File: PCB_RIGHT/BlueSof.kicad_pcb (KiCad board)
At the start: 2 copper layers, 134.8 x 98.3 mm, 88 parts, among them J1 USB_C_Receptacle_USB2.0, J12 SM02B-SRSS-TB_LF__SN_, Q2 A03407, SW1 SW_PUSH, SW10 SW_PUSH, SW11 SW_PUSH, SW12 SW_PUSH, SW13 SW_PUSH, SW14 SW_PUSH, SW15 SW_PUSH, SW16 SW_PUSH, SW17 SW_PUSH, SW18 SW_PUSH, SW19 SW_PUSH, SW2 SW_PUSH, SW20 SW_PUSH, SW21 SW_PUSH, SW22 SW_PUSH, SW23 SW_PUSH, SW24 SW_PUSH, SW25 Rotary_Encoder_Switch, SW26 SW_PUSH, SW27 SW_PUSH, SW28 SW_PUSH, SW3 SW_PUSH, SW4 SW_PUSH, SW5 SW_PUSH, SW6 SW_PUSH, SW7 SW_PUSH, SW8 SW_PUSH, SW9 SW_PUSH, U1 LN2054Y42AMR, U2 E73-2G4M08S1C, U3 AP2112K-3.3, Y1 32.768kHz

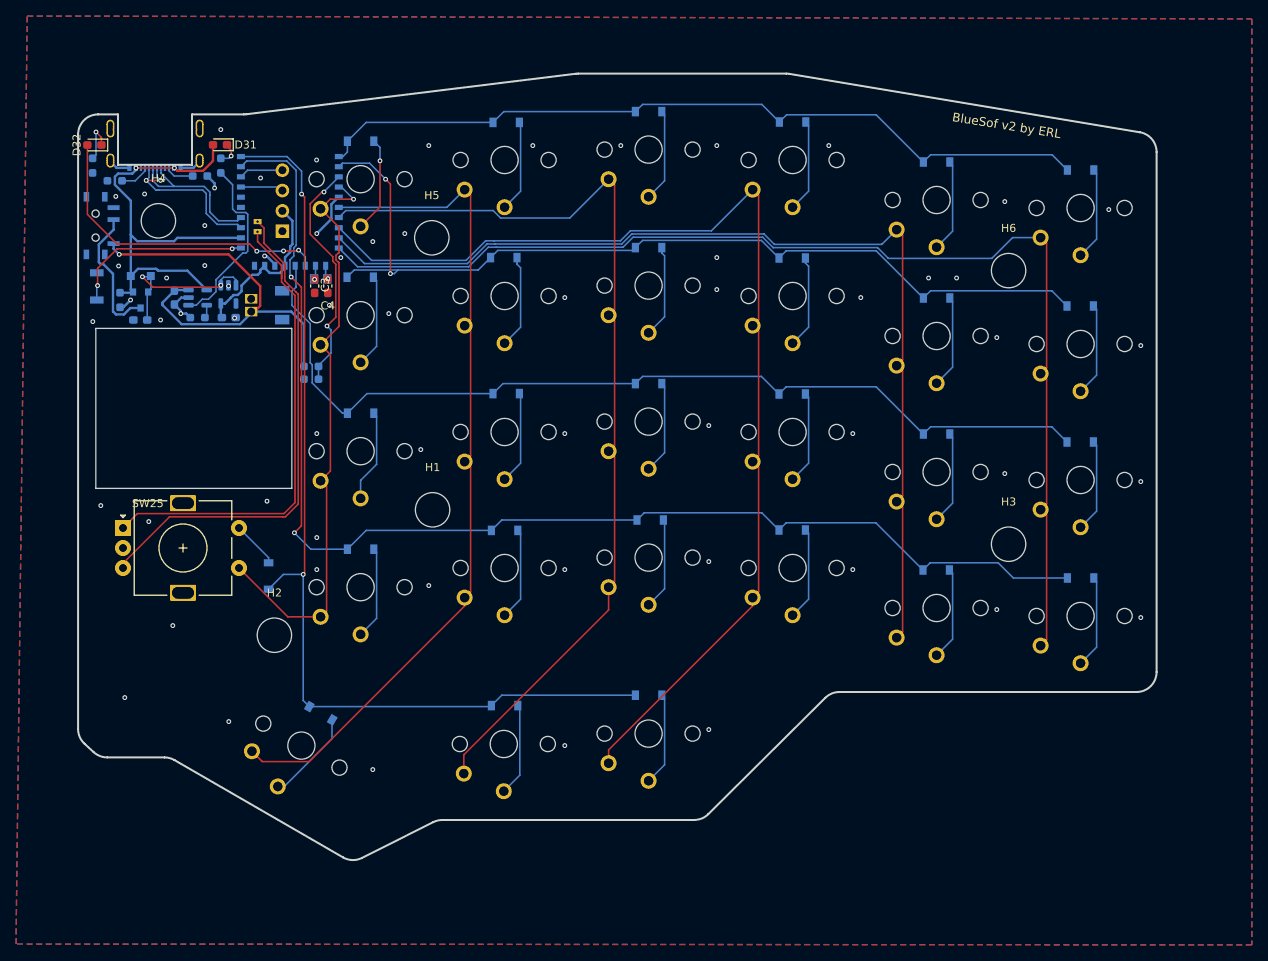
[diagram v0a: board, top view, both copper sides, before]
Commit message: ordered left side from jlc
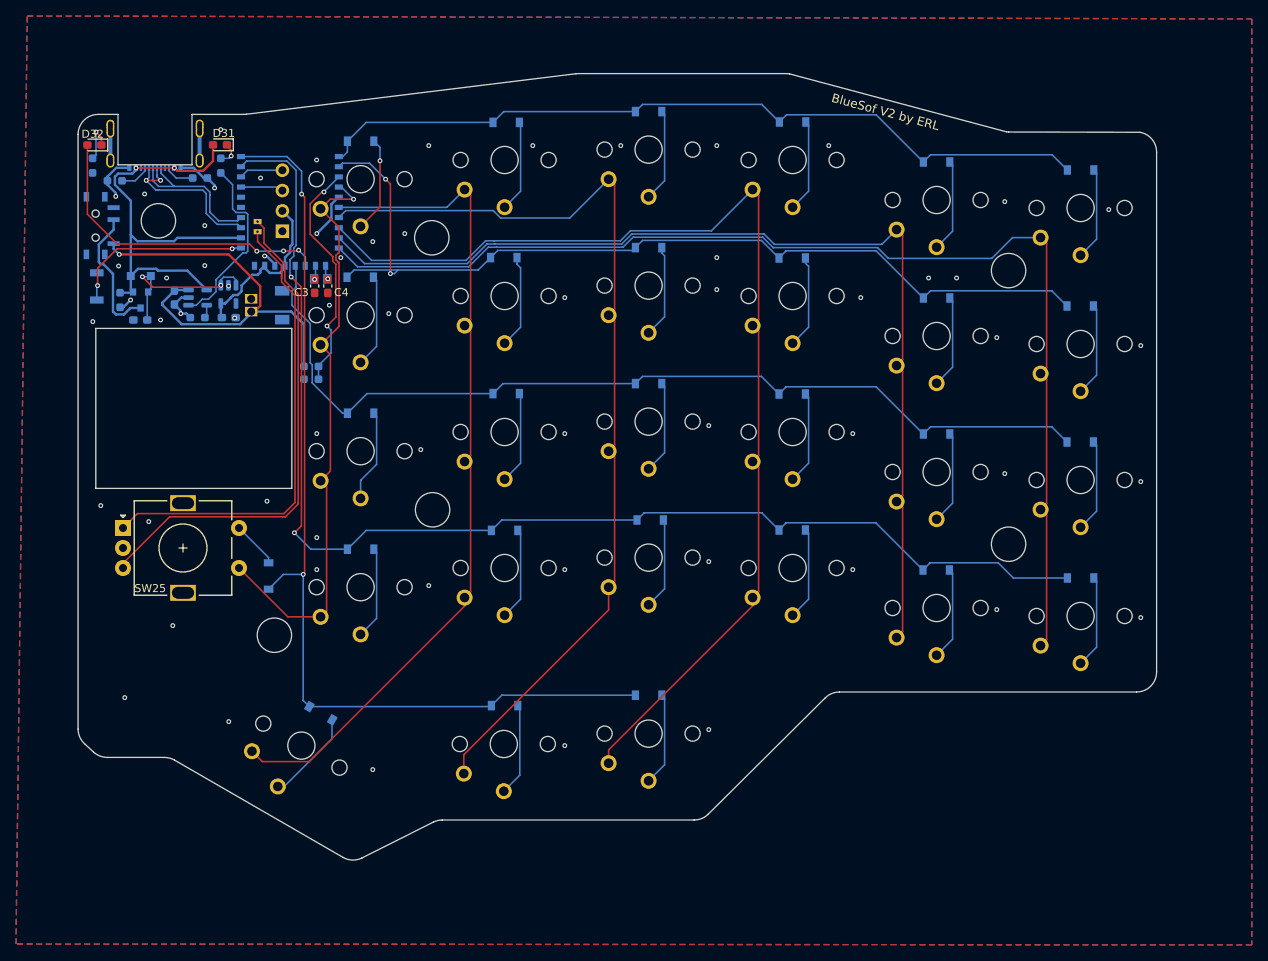
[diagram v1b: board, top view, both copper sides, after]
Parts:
- J12: value SM02B-SRSS-TB_LF__SN_ -> SM02B-SRSS-TB(LF)(SN)
- moved R8 0.25 mm to (101.4, 54.0)
- renumbered BATT1 to BATT_SW, RESET1 to RESET
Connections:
- net DATA+ renamed D+
- net DATA- renamed D-
- BATT_SW pad 3: no_connect_72 -> unconnected-(BATT1-Pad3)
- H1 pad 1: Net-(H1-Pad1) -> unconnected-(H1-Pad1)
- H2 pad 1: Net-(H2-Pad1) -> unconnected-(H2-Pad1)
- H3 pad 1: Net-(H3-Pad1) -> unconnected-(H3-Pad1)
- H4 pad 1: Net-(H4-Pad1) -> unconnected-(H4-Pad1)
- H5 pad 1: Net-(H5-Pad1) -> unconnected-(H5-Pad1)
- H6 pad 1: Net-(H6-Pad1) -> unconnected-(H6-Pad1)
- J1 pad A8: no_connect_73 -> unconnected-(J1-PadA8)
- J1 pad B8: no_connect_74 -> unconnected-(J1-PadB8)
- J1 pad S1: GND -> unconnected-(J1-PadS1)
- U2 pad 33: Net-(U2-Pad33) -> unconnected-(U2-Pad33)
- U2 pad 35: Net-(U2-Pad35) -> unconnected-(U2-Pad35)
- U3 pad 4: no_connect_87 -> unconnected-(U3-Pad4)
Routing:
- net unconnected-(J1-PadS1): track 0.00 -> 8.09 mm
- net GND: track 21.3 -> 25.7 mm
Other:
- outline, holes or cut-outs redrawn
- board text added: "BlueSof V2 by ERL"
- board text removed: "BlueSof v1 by ERL"
- board text removed: "BlueSof v2 by ERL"

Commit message: minor updates for SMD assembly
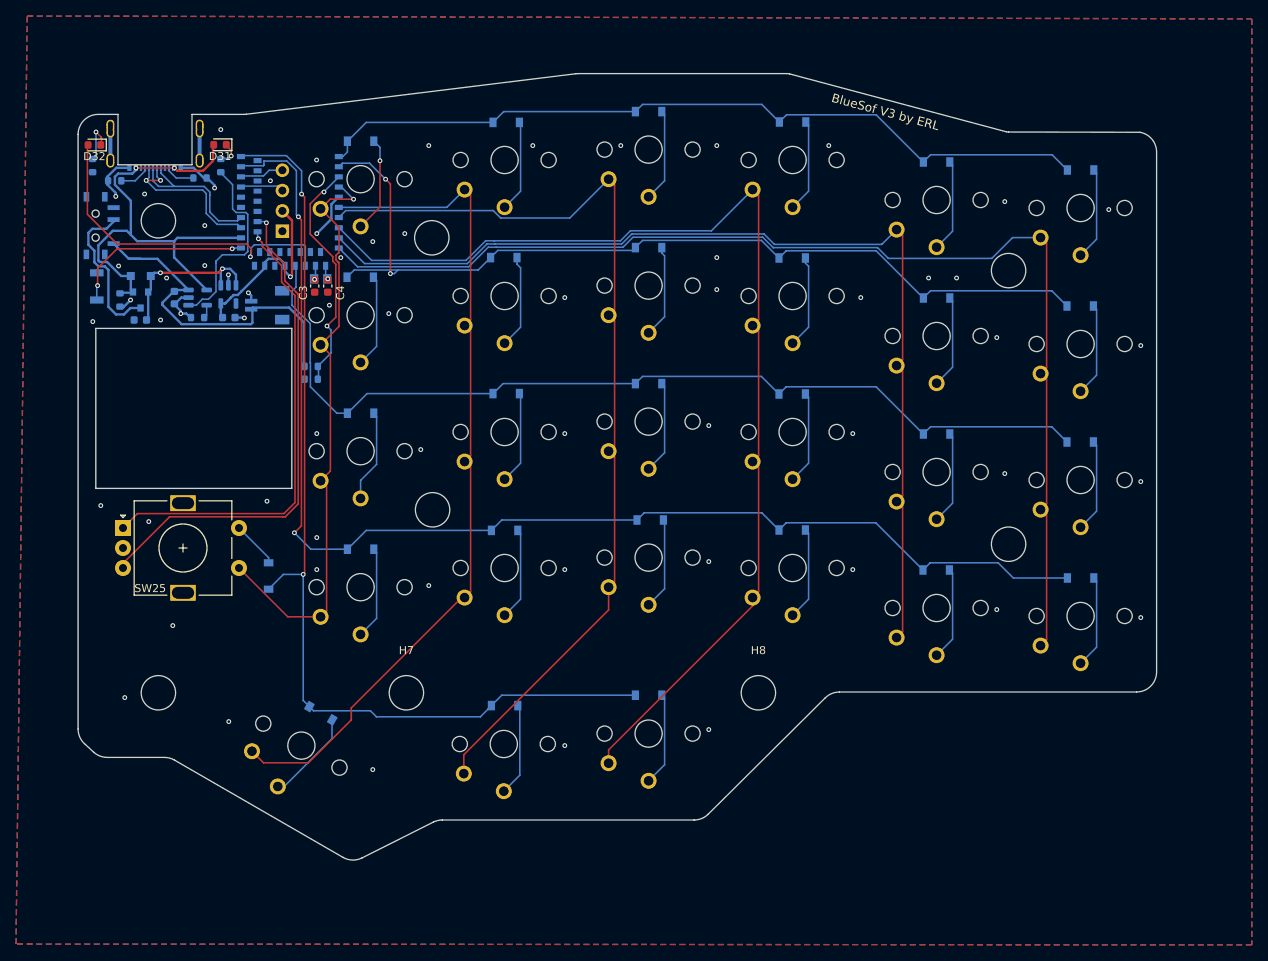
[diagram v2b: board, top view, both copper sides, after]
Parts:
- added H7: MountingHole_Pad, MountingHole:MountingHole_4.3mm_M4, F.Cu at (127.2, 118.3)
- added H8: MountingHole_Pad, MountingHole:MountingHole_4.3mm_M4, F.Cu at (171.2, 118.3)
- C1, C2, C3, C4, C5: footprint Capacitor_SMD:C_0603_1608Metric_Pad1.08x0.95mm_HandSolder -> Capacitor_SMD:C_0603_1608Metric
- D31, D32: footprint LED_SMD:LED_0603_1608Metric_Pad1.05x0.95mm_HandSolder -> LED_SMD:LED_0603_1608Metric
- R1, R2, R4, R5, R6, R7, R8, R9: footprint Resistor_SMD:R_0603_1608Metric_Pad0.98x0.95mm_HandSolder -> Resistor_SMD:R_0603_1608Metric
- U2: footprint BlueSof:E73-2G4M08S1C-52840_minimal_inside_pads -> BlueSof:E73-2G4M08S1C-52840_SMD
- moved H2 16.2 mm to (96.2, 118.3)
- renumbered BATT_SW to BATT
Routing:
- net VBAT: track 54.2 -> 44.3 mm, vias 1 -> 0
- net VBUS: track 57.7 -> 61.1 mm
- net P0.05: track 39.3 -> 42.6 mm, vias 3 -> 1
- net VDD_H: track 20.5 -> 23.2 mm, vias 0 -> 1
- net BATT_SWITCHED: track 17.1 -> 19.5 mm
- net GND: track 25.7 -> 27.7 mm
- net Net-(R1-Pad2): track 23.0 -> 24.6 mm
- net ENCA: track 60.2 -> 58.6 mm, vias 0 -> 1
- net row4: track 122.1 -> 123.3 mm
- net SWD: track 4.74 -> 5.30 mm
- net ENCB: track 62.5 -> 62.9 mm, vias 0 -> 1
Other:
- board text added: "BlueSof V3 by ERL"
- board text removed: "BlueSof V2 by ERL"

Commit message: working towards next order
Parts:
- added +: Conn_01x01_Female, Connector_PinSocket_1.27mm:PinSocket_1x01_P1.27mm_Vertical, B.Cu at (130.5, 78.7)
- added Batt: Jumper_2_Open, Jumper:SolderJumper-2_P1.3mm_Open_Pad1.0x1.5mm, B.Cu at (116.2, 85.2)
- added J2: Conn_01x01_Female, Connector_PinSocket_1.27mm:PinSocket_1x01_P1.27mm_Vertical, F.Cu at (130.5, 82.3)
- C3, C4: moved to B.Cu
- moved D1 6.06 mm to (127.1, 47.1)
- moved C3 4.33 mm to (120.1, 67.3), turned to 180 degrees
- moved C4 3.23 mm to (120.1, 65.7), turned to 180 degrees
- moved D7 3.00 mm to (124.2, 67.5)
- turned SW1 to 180 degrees
- renumbered BATT to BATT1
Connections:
- net Net-(C2-Pad1) renamed VIN
- U2 pad 12: (no net) -> unconnected-(U2-Pad12)
- U2 pad 14: (no net) -> unconnected-(U2-Pad14)
- U2 pad 16: (no net) -> unconnected-(U2-Pad16)
- U2 pad 18: (no net) -> unconnected-(U2-Pad18)
- U2 pad 20: (no net) -> unconnected-(U2-Pad20)
- U2 pad 22: (no net) -> unconnected-(U2-Pad22)
- U2 pad 24: (no net) -> GND
- U2 pad 32: (no net) -> unconnected-(U2-Pad32)
- U2 pad 34: (no net) -> unconnected-(U2-Pad34)
- U2 pad 36: (no net) -> unconnected-(U2-Pad36)
- U2 pad 38: (no net) -> unconnected-(U2-Pad38)
- U2 pad 40: (no net) -> unconnected-(U2-Pad40)
- U2 pad 42: (no net) -> unconnected-(U2-Pad42)
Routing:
- net col5: track 74.4 -> 91.8 mm, vias 1 -> 0
- net Net-(J2-Pad1): track 0.00 -> 14.9 mm
- net col0: track 145.3 -> 157.8 mm
- net VBAT: track 44.3 -> 51.4 mm
- net Net-(D1-Pad2): track 12.0 -> 7.73 mm, vias 1 -> 0
- net Net-(C3-Pad2): track 1.47 -> 5.27 mm, vias 1 -> 0
- net GND: track 27.7 -> 30.6 mm, vias 62 -> 63
- net row1: track 116.4 -> 114.2 mm
- net row0: track 99.5 -> 101.6 mm
- net Net-(C4-Pad2): track 1.44 -> 3.53 mm, vias 1 -> 0
- net BATTERY_MEASURE: track 29.4 -> 29.0 mm, vias 2 -> 0
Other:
- board text added: "BATT"
